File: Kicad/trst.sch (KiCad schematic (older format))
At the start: 21 parts, among them CN2 , J1 Conn_02x30_Odd_Even, U1 MC88916, U21 DM74AS646, U22 DM74AS646, U23 DM74AS646, U24 DM74AS646, U3 PALCE20V8H, U4 MC68040, U6 MACH130, U8 MACH110, X1 GTXO-S14V

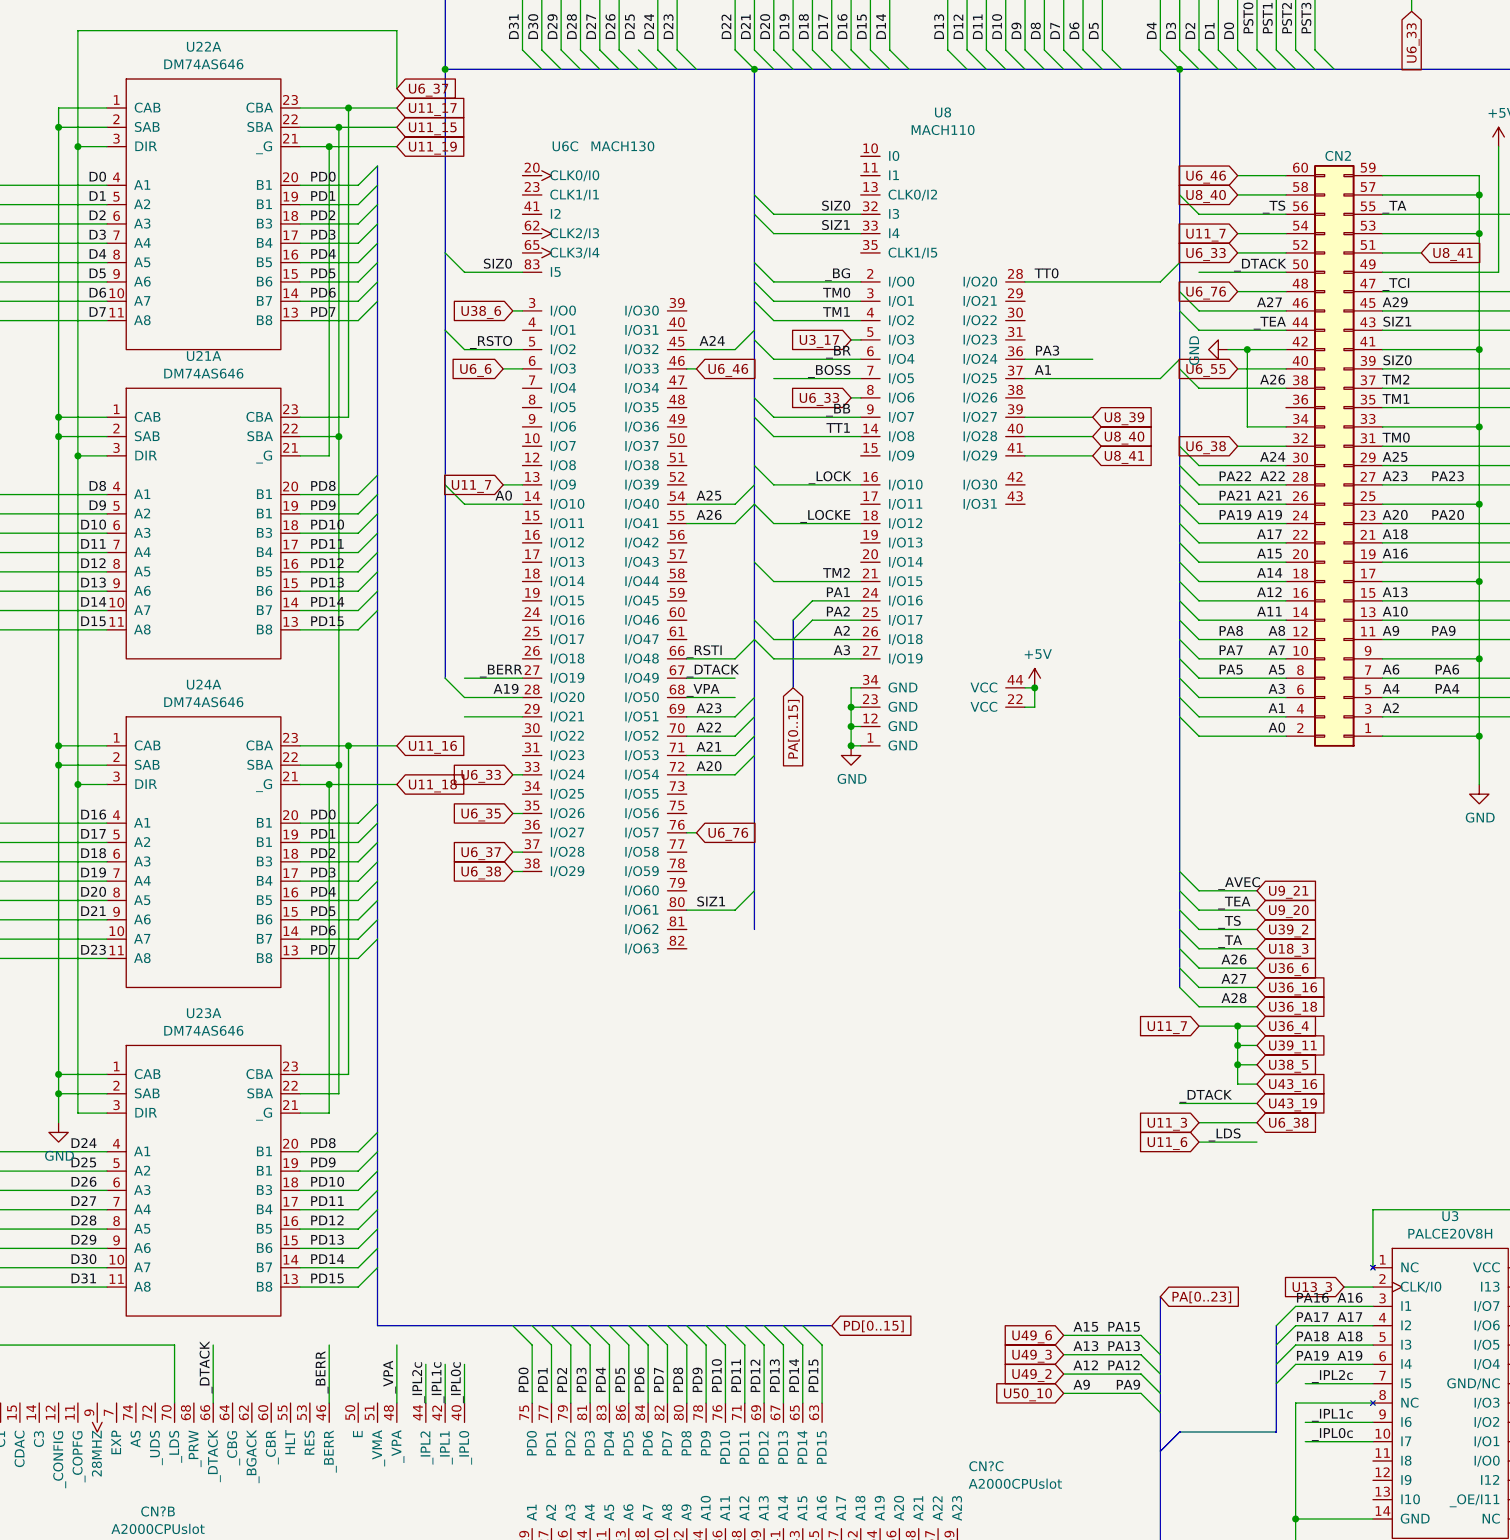
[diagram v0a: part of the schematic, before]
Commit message: some more pins and datasheets
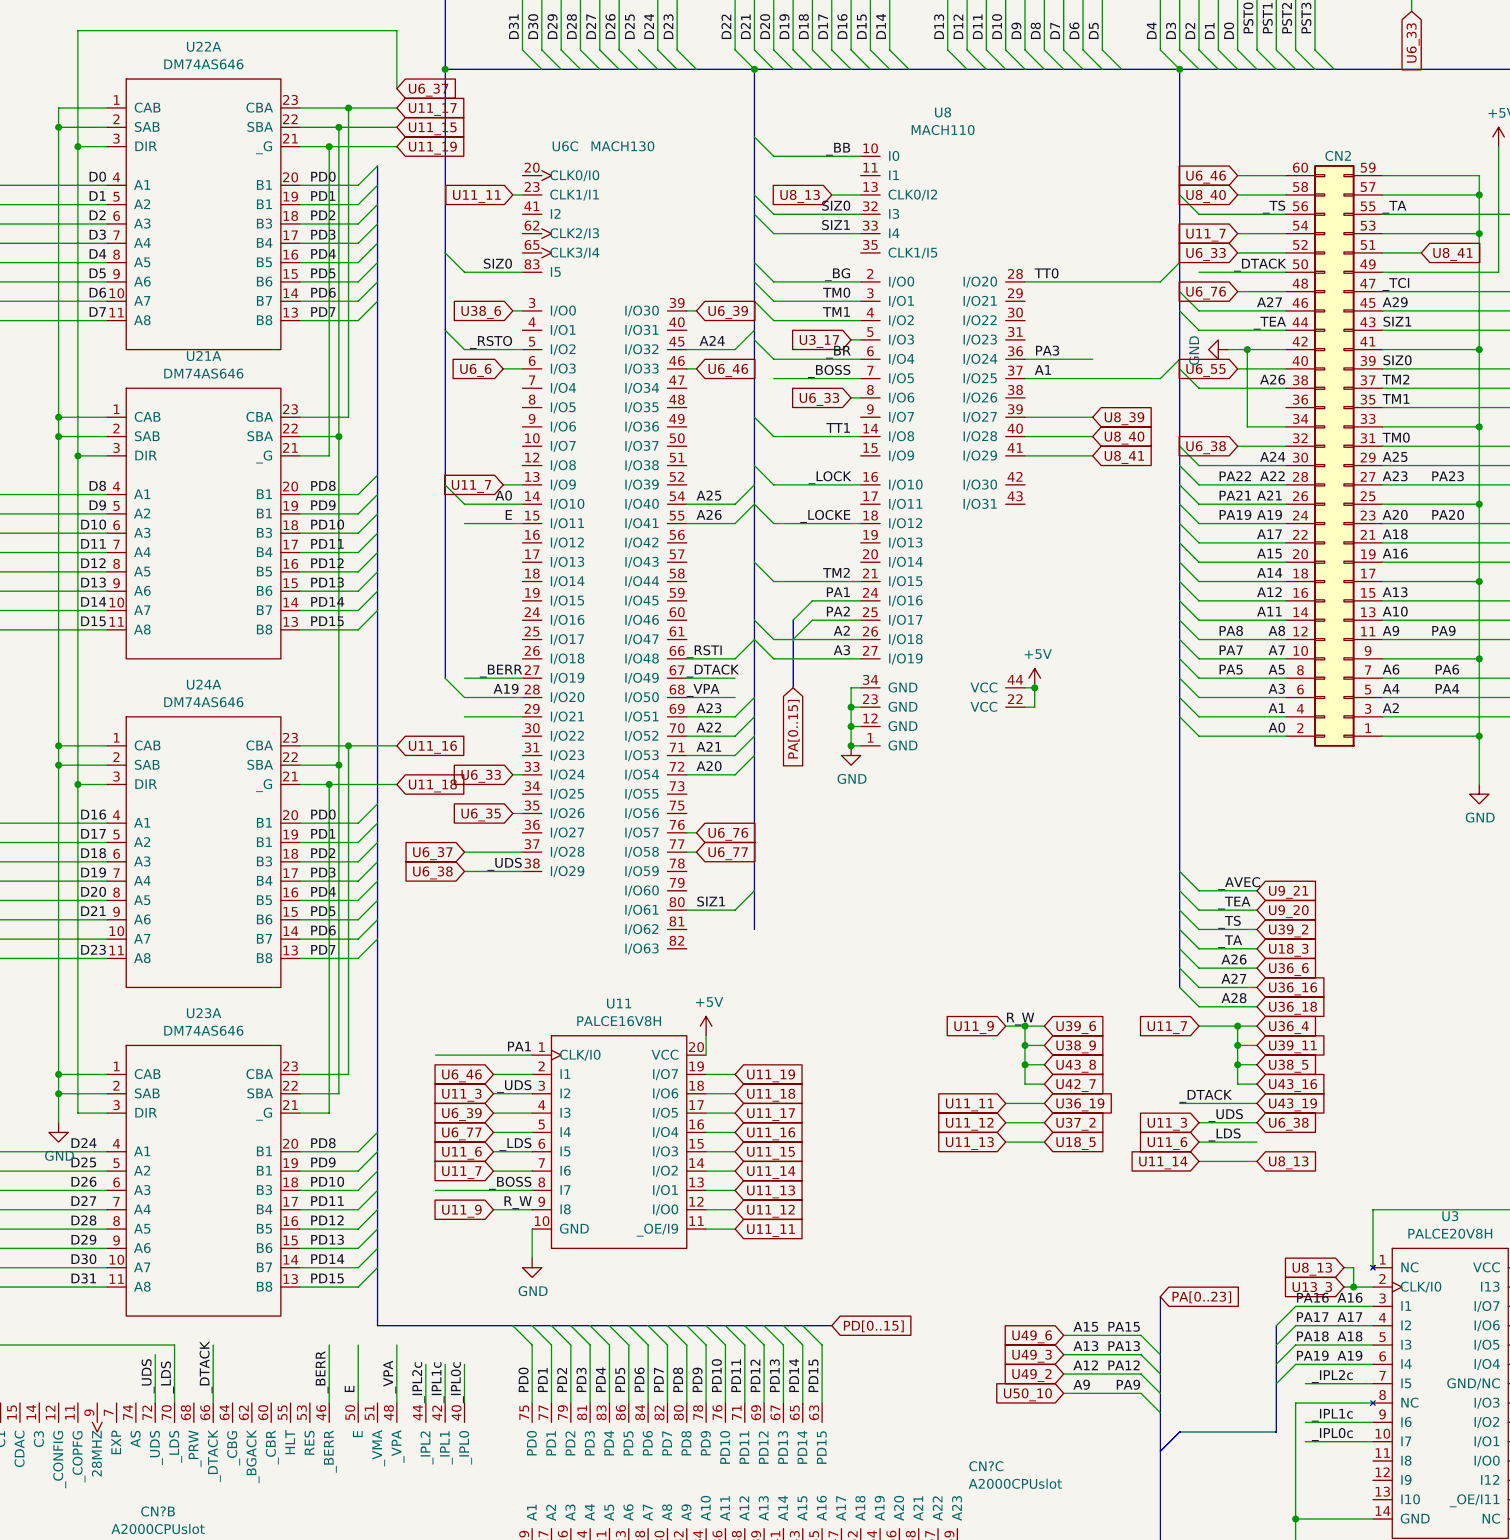
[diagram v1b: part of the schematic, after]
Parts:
- added U11: PALCE16V8H, symbol New_Library_0:PALCE16V8H
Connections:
- net U13_3 is gone; now on net U11_14: U3.2 (CLK/I0)
- net +5V: now also U11.20 (VCC)
- net GND: now also U11.10 (GND)
- net PA1: now also U11.1 (CLK/I0)
- net U11_15: now also U11.15 (I/O3)
- net U11_16: now also U11.16 (I/O4)
- net U11_17: now also U11.17 (I/O5)
- net U11_18: now also U11.18 (I/O6)
- net U11_19: now also U11.19 (I/O7)
- net U11_3: now also CN?.72 (_UDS), U11.3 (I2)
- net U11_6: now also U11.6 (I5)
- net U11_7: now also U11.7 (I6)
- net U6_46: now also U11.2 (I1)
- net _BB: now also U8.10 (I0); no longer U8.9 (I/O7)
- net _BOSS: now also U11.8 (I7)
- net E: now reaches CN?.50 (E)
- net E: now also U6.15 (I/O11)
- net U11_11: now reaches U6.23 (CLK1/I1)
- net U11_11: now also U11.11 (_OE/I9)
- net U6_39: now reaches U6.39 (I/O30)
- net U6_39: now also U11.4 (I3)
- net U6_77: now reaches U6.77 (I/O58)
- net U6_77: now also U11.5 (I4)
- net U11_14: now reaches U8.13 (CLK0/I2)
- net U11_14: now also U11.14 (I/O2)
- net R_W renamed U11_9
- net U11_9: now also U11.9 (I8)
- new net U11_12: U11.12 (I/O0)
- new net U11_13: U11.13 (I/O1)
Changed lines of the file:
@@
 U13_3
 Wire Wire Line
-	9550 8950 9700 8950
+	9550 8950 9600 8950
 Wire Wire Line
 	9700 9350 9300 9350
@@
 Wire Wire Line
 	7000 4350 7050 4350
-Text GLabel 5250 6700 0    50   Input ~ 0
+Text GLabel 5000 6700 0    50   Input ~ 0
 U6_37
-Wire Wire Line
-	5250 6700 5300 6700
 Wire Wire Line
 	3700 9550 3700 9250
@@
 Entry Wire Line
 	8800 4300 8700 4200
-Text GLabel 5250 6800 0    50   Input ~ 0
+Text GLabel 5000 6800 0    50   Input ~ 0
 U6_38
-Wire Wire Line
-	5250 6800 5300 6800
 Text GLabel 9000 4600 0    50   Input ~ 0
 U6_38
@@
 Text Label 14200 4400 0    50   ~ 0
 _BB
-Text Label 7000 4450 2    50   ~ 0
+Text Label 7000 3100 2    50   ~ 0
 _BB
-Wire Wire Line
-	6600 4450 7050 4450
-Entry Wire Line
-	6500 4350 6600 4450
 Wire Wire Line
 	4800 9550 4800 9350
@@
 	10700 9950 10500 9950
 Wire Wire Line
+	7050 3100 6600 3100
+Entry Wire Line
+	6500 3000 6600 3100
+Text GLabel 6900 3300 0    50   Input ~ 0
+U8_13
+Wire Wire Line
+	6900 3300 7050 3300
+Text GLabel 9100 8300 2    50   Input ~ 0
+U8_13
+Text GLabel 8800 8300 0    50   Input ~ 0
+U11_14
+Wire Wire Line
+	8800 8300 9100 8300
+Text GLabel 9550 8850 0    50   Input ~ 0
+U8_13
+Wire Wire Line
+	9550 8850 9600 8850
+Wire Wire Line
+	9600 8850 9600 8950
+Connection ~ 9600 8950
+Wire Wire Line
+	9600 8950 9700 8950
+$Comp
+L New_Library_0:PALCE16V8H U11
+U 1 1 5DAA9A5A
+P 5800 8250
+F 0 "U11" H 5800 9015 50  0000 C CNN
+F 1 "PALCE16V8H" H 5800 8924 50  0000 C CNN
+F 2 "" H 5800 8250 50  0001 C CNN
+F 3 "" H 5800 8250 50  0001 C CNN
+	1    5800 8250
+	1    0    0    -1
+$EndComp
+Text GLabel 6400 7950 2    50   Input ~ 0
+U11_18
+Wire Wire Line
+	6400 7950 6250 7950
+Text GLabel 6400 8150 2    50   Input ~ 0
+U11_16
+Wire Wire Line
+	6400 8150 6250 8150
+Text GLabel 6400 7850 2    50   Input ~ 0
+U11_19
+Wire Wire Line
+	6400 7850 6250 7850
+Text GLabel 6400 8250 2    50   Input ~ 0
+U11_15
+Wire Wire Line
+	6400 8250 6250 8250
+Text GLabel 6400 8050 2    50   Input ~ 0
+U11_17
+Wire Wire Line
+	6400 8050 6250 8050
+Text GLabel 5150 8350 0    50   Input ~ 0
+U11_7
+Wire Wire Line
+	5150 8350 5350 8350
+Text GLabel 5150 7950 0    50   Input ~ 0
+U11_3
+Wire Wire Line
+	5150 7950 5350 7950
+Text GLabel 5150 8250 0    50   Input ~ 0
+U11_6
+Wire Wire Line
+	5150 8250 5350 8250
+Text GLabel 6400 8350 2    50   Input ~ 0
+U11_14
+Wire Wire Line
+	6400 8350 6250 8350
+Text Label 5350 7750 2    50   ~ 0
+PA1
+Text GLabel 5150 7850 0    50   Input ~ 0
+U6_46
+Wire Wire Line
+	5150 7850 5350 7850
+Text GLabel 5150 8050 0    50   Input ~ 0
+U6_39
+Wire Wire Line
+	5150 8050 5350 8050
+Text GLabel 6200 3900 2    50   Input ~ 0
+U6_39
+Wire Wire Line
+	6200 3900 6150 3900
+Text GLabel 5150 8150 0    50   Input ~ 0
+U6_77
+Wire Wire Line
+	5150 8150 5350 8150
+Text GLabel 6200 6700 2    50   Input ~ 0
+U6_77
+Wire Wire Line
+	6200 6700 6150 6700
+Text Label 5350 8450 2    50   ~ 0
+_BOSS
+Wire Wire Line
+	5350 8450 4850 8450
+Wire Wire Line
+	4850 7750 5350 7750
+Text GLabel 5150 8550 0    50   Input ~ 0
+U11_9
+Wire Wire Line
+	5150 8550 5350 8550
+$Comp
+L power:GND #PWR?
+U 1 1 5E6EFFC6
+P 5350 8800
+F 0 "#PWR?" H 5350 8550 50  0001 C CNN
+F 1 "GND" H 5355 8627 50  0000 C CNN
+F 2 "" H 5350 8800 50  0001 C CNN
+F 3 "" H 5350 8800 50  0001 C CNN
+	1    5350 8800
+	1    0    0    -1
+$EndComp
+Wire Wire Line
+	5350 8800 5350 8650
+$Comp
+L power:+5V #PWR?
+U 1 1 5E7A32D8
+P 6250 7650
+F 0 "#PWR?" H 6250 7500 50  0001 C CNN
+F 1 "+5V" H 6265 7823 50  0000 C CNN
+F 2 "" H 6250 7650 50  0001 C CNN
+F 3 "" H 6250 7650 50  0001 C CNN
+	1    6250 7650
+	1    0    0    -1
+$EndComp
+Wire Wire Line
+	6250 7650 6250 7750
+Text Label 5350 8250 2    50   ~ 0
+_LDS
+Text GLabel 7800 7600 0    50   Input ~ 0
+U11_9
+Text GLabel 8000 7600 2    50   Input ~ 0
+U39_6
+Wire Wire Line
+	7800 7600 7900 7600
+Text GLabel 8000 7700 2    50   Input ~ 0
+U38_9
+Wire Wire Line
+	8000 7700 7900 7700
+Wire Wire Line
+	7900 7700 7900 7600
+Connection ~ 7900 7600
+Wire Wire Line
+	7900 7600 8000 7600
+Text GLabel 8000 7800 2    50   Input ~ 0
+U43_8
+Wire Wire Line
+	7900 7800 7900 7700
+Connection ~ 7900 7700
+Wire Wire Line
+	7900 7800 8000 7800
+Text GLabel 8000 7900 2    50   Input ~ 0
+U42_7
+Wire Wire Line
+	8000 7900 7900 7900
+Wire Wire Line
+	7900 7900 7900 7800
+Connection ~ 7900 7800
+Text Label 5350 8550 2    50   ~ 0
+R_W
+Text Label 7800 7600 0    50   ~ 0
+R_W
+Wire Wire Line
+	6250 8650 6400 8650
+Text GLabel 6400 8650 2    50   Input ~ 0
+U11_11
+Text GLabel 5250 3300 0    50   Input ~ 0
+U11_11
+Wire Wire Line
+	5250 3300 5300 3300
+Text GLabel 8000 8000 2    50   Input ~ 0
+U36_19
+Text GLabel 6400 8550 2    50   Input ~ 0
+U11_12
+Wire Wire Line
+	6400 8550 6250 8550
+Text GLabel 7800 8000 0    50   Input ~ 0
+U11_11
+Wire Wire Line
+	7800 8000 8000 8000
+Text GLabel 8000 8100 2    50   Input ~ 0
+U37_2
+Text GLabel 7800 8100 0    50   Input ~ 0
+U11_12
+Wire Wire Line
+	7800 8100 8000 8100
+Text GLabel 8000 8200 2    50   Input ~ 0
+U18_5
+Text GLabel 6400 8450 2    50   Input ~ 0
+U11_13
+Wire Wire Line
+	6400 8450 6250 8450
+Text GLabel 7800 8200 0    50   Input ~ 0
+U11_13
+Wire Wire Line
+	7800 8200 8000 8200
+Text Label 5350 7950 2    50   ~ 0
+_UDS
+Text Label 8850 8100 0    50   ~ 0
+_UDS
+Text Label 5300 6800 2    50   ~ 0
+_UDS
+Wire Wire Line
+	5000 6800 5300 6800
+Wire Wire Line
+	5000 6700 5300 6700
+Text Label 3500 9500 1    50   ~ 0
+_LDS
+Text Label 3400 9500 1    50   ~ 0
+_UDS
+Wire Wire Line
+	3400 9550 3400 9300
+Wire Wire Line
+	5300 5000 5000 5000
+Wire Wire Line
+	4450 9550 4450 9250
+Wire Wire Line
 	6600 5600 7050 5600
 Wire Bus Line
@@
 Wire Bus Line
 	2450 2250 2450 9000
+Text Label 4450 9500 1    50   ~ 0
+E
+Text Label 5250 5000 2    50   ~ 0
+E
 $EndSCHEMATC

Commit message: PINS... more pins
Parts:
- added JP7: U7, symbol Jumper:SolderJumper_2_Open
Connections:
- net labels added: AS, CDAC, EXP, FC0, FC1, FC2, HLT, RES, U14_11, U14_12, U14_13, U14_3, U15_11, U15_2, U16_6, U16_8, U17_11, U17_5, U17_6, U17_9, U18_4, U19_11, U19_9, U3_11, U3_12, U3_13, U3_16, U51_8, U6_20, U6_62, U6_65, U7_11, _BGACK, _CBG, _CBR, _COPFG, _PRW, _VMA
- wire segments 769 -> 831

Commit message: U9 Pinned out
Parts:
- added JP10: J10, symbol Jumper:SolderJumper_2_Open
- added U9: PAL22V10, symbol New_Library_0:PAL22V10
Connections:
- net labels added: U11_8, U14_5, U15_12, U15_9, U37_11, U37_3, U6_81, U7_1, U7_10, U7_12, U7_6, U8_11, U8_43, U9_13, U9_19, U9_2, U9_7, U9_9
- wire segments 831 -> 874
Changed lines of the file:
@@
 	5250 6300 5300 6300
 Text GLabel 7000 4350 0    50   Input ~ 0
-U6_33
+U11_8
 Wire Wire Line
 	7000 4350 7050 4350
@@
 Wire Wire Line
 	8000 6600 7800 6600
+$Comp
+L Jumper:SolderJumper_2_Open JP10
+U 1 1 5D85C670
+P 8100 2900
+F 0 "JP10" H 8100 3105 50  0000 C CNN
+F 1 "J10" H 8100 3014 50  0000 C CNN
+F 2 "" H 8100 2900 50  0001 C CNN
+F 3 "~" H 8100 2900 50  0001 C CNN
+	1    8100 2900
+	1    0    0    -1
+$EndComp
+Text GLabel 7950 2900 0    50   Input ~ 0
+U6_33
+Text GLabel 8250 2900 2    50   Input ~ 0
+U11_8
+Text GLabel 9700 6900 0    50   Input ~ 0
+U9_9
+Wire Wire Line
+	9700 6900 9800 6900
+Text GLabel 9950 6900 2    50   Input ~ 0
+U8_11
+Text GLabel 9950 7000 2    50   Input ~ 0
+U15_12
+Wire Wire Line
+	9950 7000 9800 7000
+Wire Wire Line
+	9800 7000 9800 6900
+Connection ~ 9800 6900
+Wire Wire Line
+	9800 6900 9950 6900
+Text GLabel 6900 3200 0    50   Input ~ 0
+U8_11
+Wire Wire Line
+	6900 3200 7050 3200
+Text GLabel 6900 3600 0    50   Input ~ 0
+U6_35
+Wire Wire Line
+	6900 3600 7050 3600
+Text GLabel 9700 7100 0    50   Input ~ 0
+U9_13
+Wire Wire Line
+	9700 7100 9950 7100
+Text GLabel 9950 7100 2    50   Input ~ 0
+U6_35
+$Comp
+L New_Library_0:PAL22V10 U9
+U 1 1 5DDA408D
+P 15650 8100
+F 0 "U9" H 15625 8715 50  0000 C CNN
+F 1 "PAL22V10" H 15625 8624 50  0000 C CNN
+F 2 "" H 15650 8100 50  0001 C CNN
+F 3 "" H 15650 8100 50  0001 C CNN
+	1    15650 8100
+	1    0    0    -1
+$EndComp
+Text GLabel 15050 8550 0    50   Input ~ 0
+U9_9
+Wire Wire Line
+	15050 8550 15200 8550
+Text GLabel 15050 8950 0    50   Input ~ 0
+U9_13
+Wire Wire Line
+	15050 8950 15200 8950
+Text GLabel 16250 8450 2    50   Input ~ 0
+U9_21
+Wire Wire Line
+	16250 8450 16050 8450
+Text Label 16050 8450 0    50   ~ 0
+_AVEC
+Text GLabel 16250 8550 2    50   Input ~ 0
+U9_20
+Wire Wire Line
+	16250 8550 16050 8550
+Text Label 16050 8550 0    50   ~ 0
+_TEA
+Text GLabel 15050 7950 0    50   Input ~ 0
+U9_3
+Wire Wire Line
+	15050 7950 15200 7950
+$Comp
+L power:GND #PWR?
+U 1 1 5E2163C1
+P 15200 9150
+F 0 "#PWR?" H 15200 8900 50  0001 C CNN
+F 1 "GND" H 15205 8977 50  0000 C CNN
+F 2 "" H 15200 9150 50  0001 C CNN
+F 3 "" H 15200 9150 50  0001 C CNN
+	1    15200 9150
+	1    0    0    -1
+$EndComp
+Wire Wire Line
+	15200 9150 15200 9050
+$Comp
+L power:+5V #PWR?
+U 1 1 5E2F9A59
+P 16100 7600
+F 0 "#PWR?" H 16100 7450 50  0001 C CNN
+F 1 "+5V" H 16115 7773 50  0000 C CNN
+F 2 "" H 16100 7600 50  0001 C CNN
+F 3 "" H 16100 7600 50  0001 C CNN
+	1    16100 7600
+	1    0    0    -1
+$EndComp
+Wire Wire Line
+	16100 7600 16100 7750
+Wire Wire Line
+	16100 7750 16050 7750
+Text GLabel 9700 7200 0    50   Input ~ 0
+U9_2
+Wire Wire Line
+	9700 7200 9800 7200
+Text GLabel 9950 7200 2    50   Input ~ 0
+U15_9
+Text GLabel 9950 7300 2    50   Input ~ 0
+U37_3
+Text GLabel 9950 7400 2    50   Input ~ 0
+U37_11
+Wire Wire Line
+	9950 7400 9800 7400
+Wire Wire Line
+	9800 7400 9800 7300
+Connection ~ 9800 7200
+Wire Wire Line
+	9800 7200 9950 7200
+Wire Wire Line
+	9950 7300 9800 7300
+Connection ~ 9800 7300
+Wire Wire Line
+	9800 7300 9800 7200
+Text GLabel 15050 7850 0    50   Input ~ 0
+U9_2
+Wire Wire Line
+	15050 7850 15200 7850
+Text Label 15200 8050 2    50   ~ 0
+SIZ0
+Wire Wire Line
+	15200 8050 14750 8050
+Text Label 15200 8150 2    50   ~ 0
+SIZ1
+Wire Wire Line
+	15200 8150 14750 8150
+Wire Wire Line
+	7900 4900 8250 4900
+Text GLabel 8250 4900 2    50   Input ~ 0
+U8_43
+Text GLabel 15050 8250 0    50   Input ~ 0
+U8_43
+Wire Wire Line
+	15050 8250 15200 8250
+Text GLabel 15050 8350 0    50   Input ~ 0
+U9_7
+Wire Wire Line
+	15050 8350 15200 8350
+Text GLabel 9700 7500 0    50   Input ~ 0
+U9_7
+Wire Wire Line
+	9700 7500 9800 7500
+Text GLabel 9950 7500 2    50   Input ~ 0
+U7_6
+Text GLabel 9950 7600 2    50   Input ~ 0
+U7_12
+Wire Wire Line
+	9950 7600 9800 7600
+Wire Wire Line
+	9800 7600 9800 7500
+Connection ~ 9800 7500
+Wire Wire Line
+	9800 7500 9950 7500
+Text GLabel 15050 8650 0    50   Input ~ 0
+U14_5
+Wire Wire Line
+	15050 8650 15200 8650
+Text GLabel 15050 8750 0    50   Input ~ 0
+U6_39
+Text Label 15200 8750 2    50   ~ 0
+AS
+Wire Wire Line
+	15050 8750 15200 8750
+Text GLabel 6200 7100 2    50   Input ~ 0
+U6_81
+Wire Wire Line
+	6200 7100 6150 7100
+Text GLabel 15050 8850 0    50   Input ~ 0
+U6_81
+Wire Wire Line
+	15050 8850 15200 8850
+Text GLabel 16250 8650 2    50   Input ~ 0
+U9_19
+Wire Wire Line
+	16250 8650 16050 8650
+Text GLabel 9700 7700 0    50   Input ~ 0
+U9_19
+Wire Wire Line
+	9700 7700 9800 7700
+Text GLabel 9950 7700 2    50   Input ~ 0
+U7_1
+Text GLabel 9950 7800 2    50   Input ~ 0
+U7_10
+Wire Wire Line
+	9950 7800 9800 7800
+Wire Wire Line
+	9800 7800 9800 7700
+Connection ~ 9800 7700
+Wire Wire Line
+	9800 7700 9950 7700
+Wire Wire Line
+	16050 8150 16250 8150
+Text Label 16050 8150 0    50   ~ 0
+_TCI
+Wire Wire Line
+	16050 8050 16250 8050
+Text Label 16050 8050 0    50   ~ 0
+_TBI
+Text GLabel 16250 7950 2    50   Input ~ 0
+U18_3
+Wire Wire Line
+	16250 7950 16050 7950
 Wire Wire Line
 	6600 5600 7050 5600
